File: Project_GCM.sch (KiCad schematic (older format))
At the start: 21 parts, among them J1 PowerSupply, J12 DEBUG_BUSES, J7 3-641124-6, U1 LM810, U11 74AHC1G04, U2 LTC6994xS6-1, U25 74AHC1G32, U3 74AHC1G32, U5 74AHC1G04

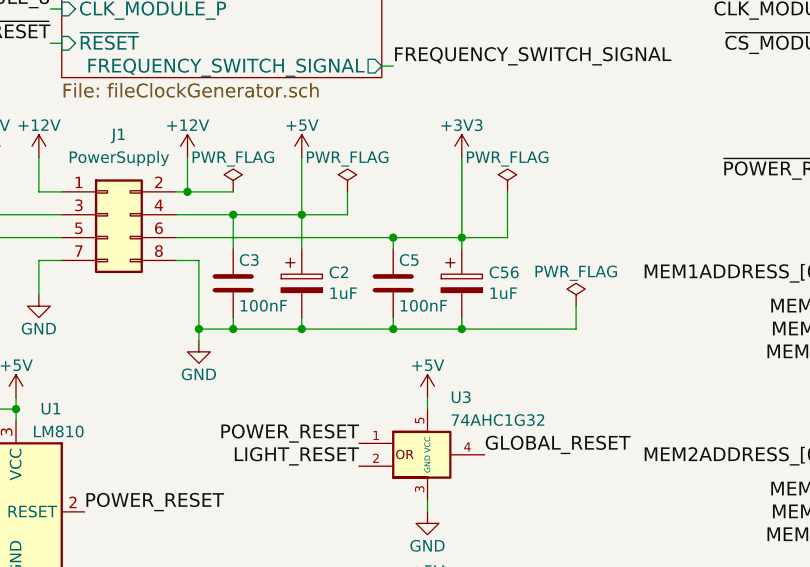
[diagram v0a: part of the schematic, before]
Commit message: Put non-electrolytic capacitor #10
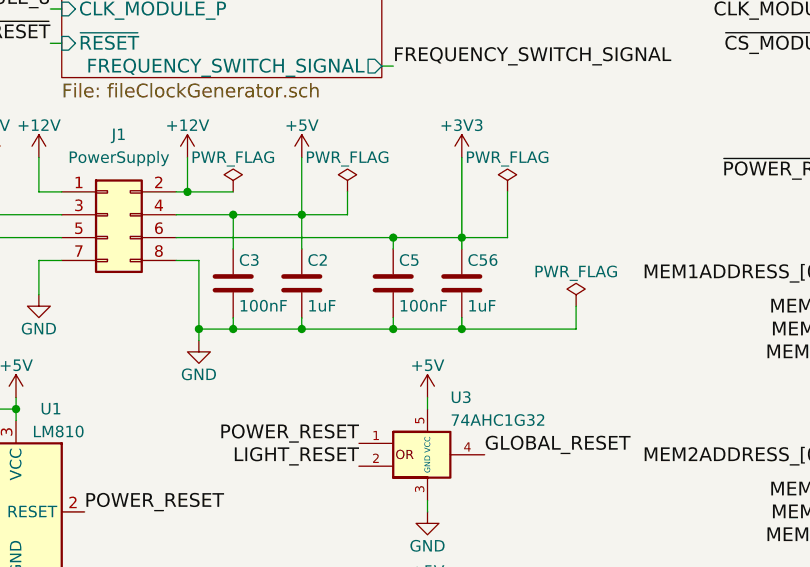
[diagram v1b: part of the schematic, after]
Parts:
- removed C2, C56: 1uF, symbol Device:C_Polarized
- added C2, C56: 1uF, Capacitor_SMD:C_0805_2012Metric, symbol Device:C
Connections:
- net +3V3: now also C56.1
- net +5V: now also C2.1
- net GND: now also C2.2, C56.2
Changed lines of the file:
@@
 Wire Wire Line
 	1900 4250 2050 4250
-$Comp
-L Device:C_Polarized C2
-U 1 1 602E7921
-P 2350 4050
-F 0 "C2" H 2468 4096 50  0000 L CNN
-F 1 "1uF" H 2468 4005 50  0000 L CNN
-F 2 "" H 2388 3900 50  0001 C CNN
-F 3 "~" H 2350 4050 50  0001 C CNN
-	1    2350 4050
-	1    0    0    -1
-$EndComp
-$Comp
-L Device:C_Polarized C56
-U 1 1 60310A8D
-P 3050 4050
-F 0 "C56" H 3168 4096 50  0000 L CNN
-F 1 "1uF" H 3168 4005 50  0000 L CNN
-F 2 "" H 3088 3900 50  0001 C CNN
-F 3 "~" H 3050 4050 50  0001 C CNN
-	1    3050 4050
-	1    0    0    -1
-$EndComp
 Wire Wire Line
 	2350 4250 2750 4250
@@
 Wire Wire Line
 	3050 4250 3550 4250
+$Comp
+L Device:C C2
+U 1 1 602BE1AD
+P 2350 4050
+F 0 "C2" H 2375 4150 50  0000 L CNN
+F 1 "1uF" H 2375 3950 50  0000 L CNN
+F 2 "Capacitor_SMD:C_0805_2012Metric" H 2388 3900 50  0001 C CNN
+F 3 "" H 2350 4050 50  0001 C CNN
+	1    2350 4050
+	1    0    0    -1
+$EndComp
+$Comp
+L Device:C C56
+U 1 1 602C9002
+P 3050 4050
+F 0 "C56" H 3075 4150 50  0000 L CNN
+F 1 "1uF" H 3075 3950 50  0000 L CNN
+F 2 "Capacitor_SMD:C_0805_2012Metric" H 3088 3900 50  0001 C CNN
+F 3 "" H 3050 4050 50  0001 C CNN
+	1    3050 4050
+	1    0    0    -1
+$EndComp
 Wire Bus Line
 	9000 1750 9000 2500

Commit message: Set every capacitor size to 0805
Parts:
- C4: footprint Capacitor_SMD:C_1206_3216Metric -> Capacitor_SMD:C_0805_2012Metric
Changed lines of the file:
@@
 F 0 "C4" H 2375 6450 50  0000 L CNN
 F 1 "100nF" H 2375 6250 50  0000 L CNN
-F 2 "Capacitor_SMD:C_1206_3216Metric" H 2388 6200 50  0001 C CNN
+F 2 "Capacitor_SMD:C_0805_2012Metric" H 2388 6200 50  0001 C CNN
 F 3 "" H 2350 6350 50  0001 C CNN
 	1    2350 6350

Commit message: Add new footprint for J7 TE_3-641124-6 #6
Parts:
- J7: footprint Connector_PinSocket_2.54mm:PinSocket_1x06_P2.54mm_Vertical -> TE_3-641124-6:TE_3-641124-6
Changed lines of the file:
@@
 F 0 "J7" H 8200 5350 50  0000 C CNN
 F 1 " 3-641124-6" H 8350 5450 50  0000 C CNN
-F 2 "Connector_PinSocket_2.54mm:PinSocket_1x06_P2.54mm_Vertical" H 8300 5850 50  0001 C CNN
+F 2 "TE_3-641124-6:TE_3-641124-6" H 8300 5850 50  0001 C CNN
 F 3 "~" H 8300 5850 50  0001 C CNN
 	1    8300 5850

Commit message: Schematic : set pinHeader on J12 #4
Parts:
- J12: footprint Connector_PinSocket_2.54mm:PinSocket_2x21_P2.54mm_Vertical -> Connector_PinHeader_2.54mm:PinHeader_2x21_P2.54mm_Vertical
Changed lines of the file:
@@
 F 0 "J12" H 9950 3850 50  0000 C CNN
 F 1 "DEBUG_BUSES" H 9900 3950 50  0000 C CNN
-F 2 "Connector_PinSocket_2.54mm:PinSocket_2x21_P2.54mm_Vertical" H 9900 5100 50  0001 C CNN
+F 2 "Connector_PinHeader_2.54mm:PinHeader_2x21_P2.54mm_Vertical" H 9900 5100 50  0001 C CNN
 F 3 "~" H 9900 5100 50  0001 C CNN
 	1    9900 5100

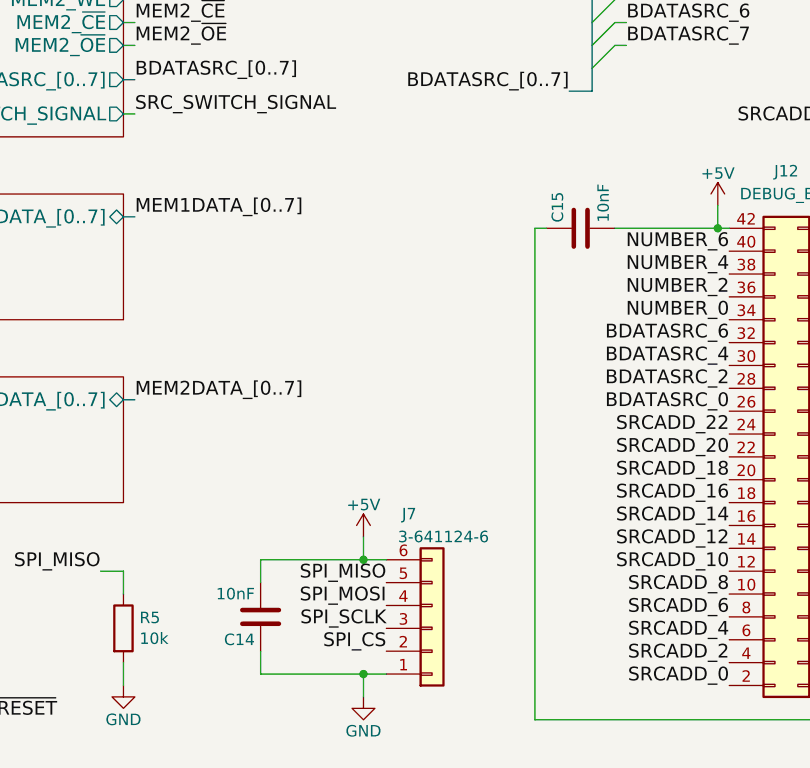
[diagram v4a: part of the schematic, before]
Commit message: Better decoupling
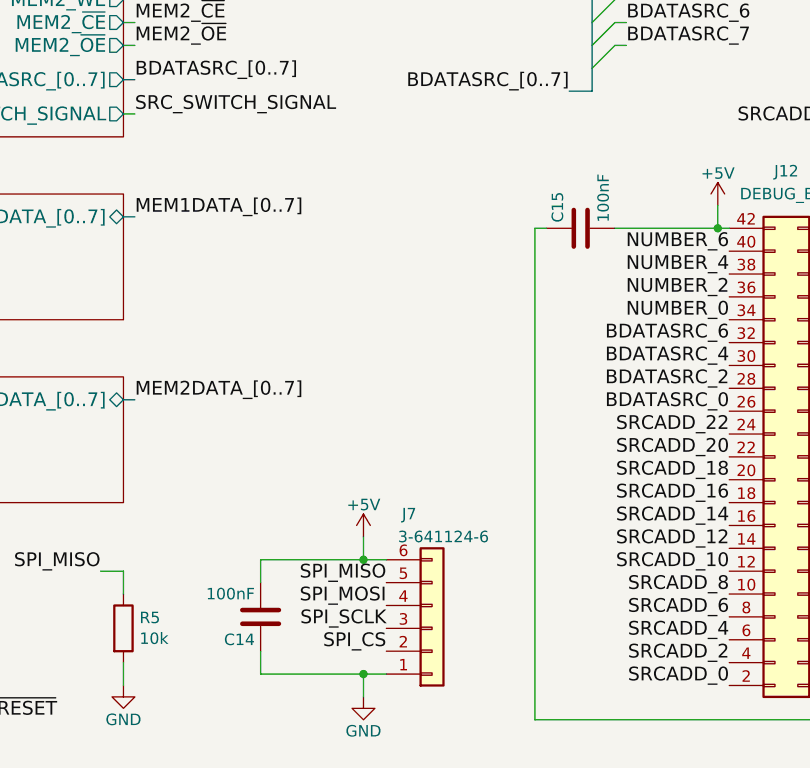
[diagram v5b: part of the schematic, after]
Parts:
- C14, C15: value 10nF -> 100nF
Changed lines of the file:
@@
 P 8950 4100
 F 0 "C15" H 8975 4200 50  0000 L CNN
-F 1 "10nF" H 8975 4000 50  0000 L CNN
+F 1 "100nF" H 8975 4000 50  0000 L CNN
 F 2 "Capacitor_SMD:C_0805_2012Metric" H 8988 3950 50  0001 C CNN
 F 3 "" H 8950 4100 50  0001 C CNN
@@
 P 7550 5800
 F 0 "C14" H 7575 5900 50  0000 L CNN
-F 1 "10nF" H 7575 5700 50  0000 L CNN
+F 1 "100nF" H 7575 5700 50  0000 L CNN
 F 2 "Capacitor_SMD:C_0805_2012Metric" H 7588 5650 50  0001 C CNN
 F 3 "" H 7550 5800 50  0001 C CNN

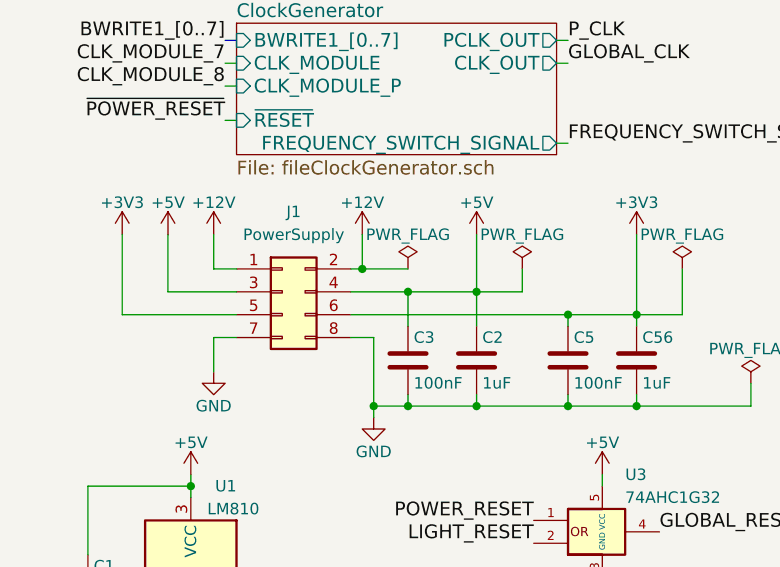
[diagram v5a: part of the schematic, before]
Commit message: Precise the molex connector for power supply
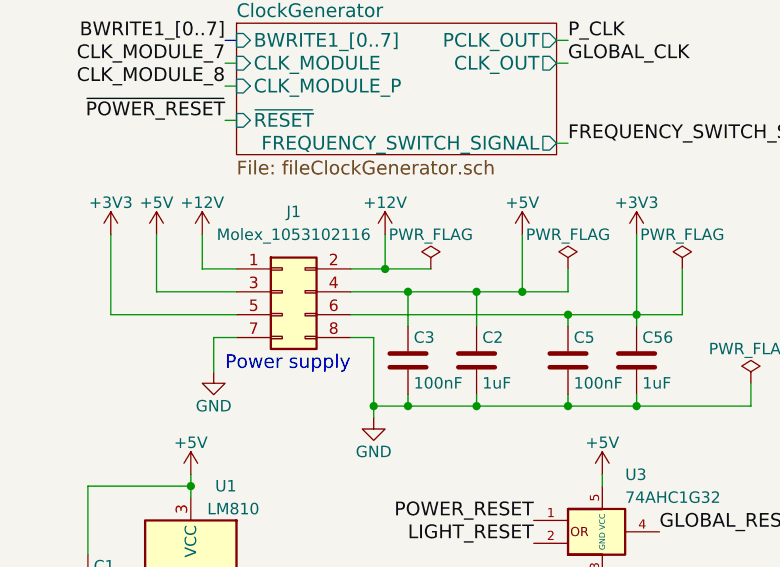
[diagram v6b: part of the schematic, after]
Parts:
- J1: value PowerSupply -> Molex_1053102116
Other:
- note added: "Power supply"
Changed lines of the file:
@@
 L power:+12V #PWR01
 U 1 1 5B3CC2AA
-P 1850 3500
-F 0 "#PWR01" H 1850 3350 50  0001 C CNN
-F 1 "+12V" H 1850 3640 50  0000 C CNN
-F 2 "" H 1850 3500 50  0001 C CNN
-F 3 "" H 1850 3500 50  0001 C CNN
-	1    1850 3500
+P 1950 3500
+F 0 "#PWR01" H 1950 3350 50  0001 C CNN
+F 1 "+12V" H 1950 3640 50  0000 C CNN
+F 2 "" H 1950 3500 50  0001 C CNN
+F 3 "" H 1950 3500 50  0001 C CNN
+	1    1950 3500
 	1    0    0    -1
 $EndComp
@@
 L power:+5V #PWR02
 U 1 1 5B3CE793
-P 2350 3500
-F 0 "#PWR02" H 2350 3350 50  0001 C CNN
-F 1 "+5V" H 2350 3640 50  0000 C CNN
-F 2 "" H 2350 3500 50  0001 C CNN
-F 3 "" H 2350 3500 50  0001 C CNN
-	1    2350 3500
+P 2550 3500
+F 0 "#PWR02" H 2550 3350 50  0001 C CNN
+F 1 "+5V" H 2550 3640 50  0000 C CNN
+F 2 "" H 2550 3500 50  0001 C CNN
+F 3 "" H 2550 3500 50  0001 C CNN
+	1    2550 3500
 	1    0    0    -1
 $EndComp
@@
 L power:+12V #PWR04
 U 1 1 5B3D12FA
-P 1200 3500
-F 0 "#PWR04" H 1200 3350 50  0001 C CNN
-F 1 "+12V" H 1200 3640 50  0000 C CNN
-F 2 "" H 1200 3500 50  0001 C CNN
-F 3 "" H 1200 3500 50  0001 C CNN
-	1    1200 3500
+P 1150 3500
+F 0 "#PWR04" H 1150 3350 50  0001 C CNN
+F 1 "+12V" H 1150 3640 50  0000 C CNN
+F 2 "" H 1150 3500 50  0001 C CNN
+F 3 "" H 1150 3500 50  0001 C CNN
+	1    1150 3500
 	-1   0    0    -1
 $EndComp
@@
 L power:+5V #PWR05
 U 1 1 5B3D1300
-P 1000 3500
-F 0 "#PWR05" H 1000 3350 50  0001 C CNN
-F 1 "+5V" H 1000 3640 50  0000 C CNN
-F 2 "" H 1000 3500 50  0001 C CNN
-F 3 "" H 1000 3500 50  0001 C CNN
-	1    1000 3500
+P 950 3500
+F 0 "#PWR05" H 950 3350 50  0001 C CNN
+F 1 "+5V" H 950 3640 50  0000 C CNN
+F 2 "" H 950 3500 50  0001 C CNN
+F 3 "" H 950 3500 50  0001 C CNN
+	1    950  3500
 	-1   0    0    -1
 $EndComp
@@
 L power:+3V3 #PWR06
 U 1 1 5B3D1306
-P 800 3500
-F 0 "#PWR06" H 800 3350 50  0001 C CNN
-F 1 "+3V3" H 800 3640 50  0000 C CNN
-F 2 "" H 800 3500 50  0001 C CNN
-F 3 "" H 800 3500 50  0001 C CNN
-	1    800  3500
+P 750 3500
+F 0 "#PWR06" H 750 3350 50  0001 C CNN
+F 1 "+3V3" H 750 3640 50  0000 C CNN
+F 2 "" H 750 3500 50  0001 C CNN
+F 3 "" H 750 3500 50  0001 C CNN
+	1    750  3500
 	-1   0    0    -1
 $EndComp
 Wire Wire Line
-	1200 3500 1200 3650
-Wire Wire Line
-	1000 3750 1300 3750
-Wire Wire Line
-	800  3500 800  3850
-Wire Wire Line
-	800  3850 1300 3850
+	1150 3500 1150 3650
+Wire Wire Line
+	750  3500 750  3850
 Wire Wire Line
 	1800 3750 2050 3750
@@
 $EndComp
 Wire Wire Line
-	1850 3650 1850 3500
-Wire Wire Line
-	2350 3750 2350 3500
+	1950 3650 1950 3500
+Wire Wire Line
+	2550 3750 2550 3500
 Wire Wire Line
 	3050 3850 3050 3500
@@
 L power:PWR_FLAG #FLG020
 U 1 1 5C78547A
-P 2050 3650
-F 0 "#FLG020" H 2050 3725 50  0001 C CNN
-F 1 "PWR_FLAG" H 2050 3800 50  0000 C CNN
-F 2 "" H 2050 3650 50  0001 C CNN
-F 3 "" H 2050 3650 50  0001 C CNN
-	1    2050 3650
+P 2150 3650
+F 0 "#FLG020" H 2150 3725 50  0001 C CNN
+F 1 "PWR_FLAG" H 2150 3800 50  0000 C CNN
+F 2 "" H 2150 3650 50  0001 C CNN
+F 3 "" H 2150 3650 50  0001 C CNN
+	1    2150 3650
 	1    0    0    -1
 $EndComp
@@
 L power:PWR_FLAG #FLG021
 U 1 1 5C7864CD
-P 2550 3650
-F 0 "#FLG021" H 2550 3725 50  0001 C CNN
-F 1 "PWR_FLAG" H 2550 3800 50  0000 C CNN
-F 2 "" H 2550 3650 50  0001 C CNN
-F 3 "" H 2550 3650 50  0001 C CNN
-	1    2550 3650
+P 2750 3650
+F 0 "#FLG021" H 2750 3725 50  0001 C CNN
+F 1 "PWR_FLAG" H 2750 3800 50  0000 C CNN
+F 2 "" H 2750 3650 50  0001 C CNN
+F 3 "" H 2750 3650 50  0001 C CNN
+	1    2750 3650
 	1    0    0    -1
 $EndComp
@@
 P 1500 3750
 F 0 "J1" H 1550 4100 50  0000 C CNN
-F 1 "PowerSupply" H 1550 4000 50  0000 C CNN
+F 1 "Molex_1053102116" H 1550 4000 50  0000 C CNN
 F 2 "Connector_Molex:Molex_Nano-Fit_105310-xx08_2x04_P2.50mm_Vertical" H 1500 3750 50  0001 C CNN
 F 3 "~" H 1500 3750 50  0001 C CNN
@@
 NoConn ~ 6500 1700
 Wire Wire Line
-	1800 3650 1850 3650
-Wire Wire Line
 	1900 4250 2050 4250
 Wire Wire Line
@@
 Wire Wire Line
 	1800 3850 2750 3850
-Connection ~ 1850 3650
-Wire Wire Line
-	1850 3650 2050 3650
+Wire Wire Line
+	1950 3650 2150 3650
 Wire Wire Line
 	2350 3750 2550 3750
 Wire Wire Line
-	2550 3750 2550 3650
+	2750 3750 2750 3650
 Wire Wire Line
 	3050 3850 3250 3850
@@
 	3250 3850 3250 3650
 Wire Wire Line
-	1200 3650 1300 3650
-Wire Wire Line
-	1000 3750 1000 3500
+	950  3750 950  3500
 Wire Wire Line
 	3550 4250 3550 4150
@@
 	1    0    0    -1
 $EndComp
+Wire Wire Line
+	1150 3650 1300 3650
+Wire Wire Line
+	950  3750 1300 3750
+Wire Wire Line
+	750  3850 1300 3850
+Wire Wire Line
+	1800 3650 1950 3650
+Connection ~ 1950 3650
+Wire Wire Line
+	2550 3750 2750 3750
 Wire Bus Line
 	9000 1750 9000 2500
@@
 Wire Bus Line
 	10400 1250 10400 3650
+Connection ~ 2550 3750
+Text Notes 1250 4100 0    60   ~ 0
+Power supply
 $EndSCHEMATC
